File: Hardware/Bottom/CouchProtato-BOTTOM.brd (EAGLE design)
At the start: 0 parts

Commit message: update files
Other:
- board outline added: 160 x 100 mm
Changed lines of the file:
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@@
 <layer number="51" name="tDocu" color="7" fill="1" visible="yes" active="yes"/>
 <layer number="52" name="bDocu" color="7" fill="1" visible="yes" active="yes"/>
+<layer number="88" name="SimResults" color="9" fill="1" visible="no" active="no"/>
+<layer number="89" name="SimProbes" color="9" fill="1" visible="no" active="no"/>
+<layer number="90" name="Modules" color="5" fill="1" visible="no" active="no"/>
+<layer number="91" name="Nets" color="2" fill="1" visible="no" active="no"/>
+<layer number="92" name="Busses" color="1" fill="1" visible="no" active="no"/>
+<layer number="93" name="Pins" color="2" fill="1" visible="no" active="no"/>
+<layer number="94" name="Symbols" color="4" fill="1" visible="no" active="no"/>
+<layer number="95" name="Names" color="7" fill="1" visible="no" active="no"/>
+<layer number="96" name="Values" color="7" fill="1" visible="no" active="no"/>
+<layer number="97" name="Info" color="7" fill="1" visible="no" active="no"/>
+<layer number="98" name="Guide" color="6" fill="1" visible="no" active="no"/>
 </layers>
 <board>
 <plain>
+<wire x1="0" y1="0" x2="160" y2="0" width="0" layer="20"/>
+<wire x1="160" y1="0" x2="160" y2="100" width="0" layer="20"/>
+<wire x1="160" y1="100" x2="0" y2="100" width="0" layer="20"/>
+<wire x1="0" y1="100" x2="0" y2="0" width="0" layer="20"/>
 </plain>
 <attributes>

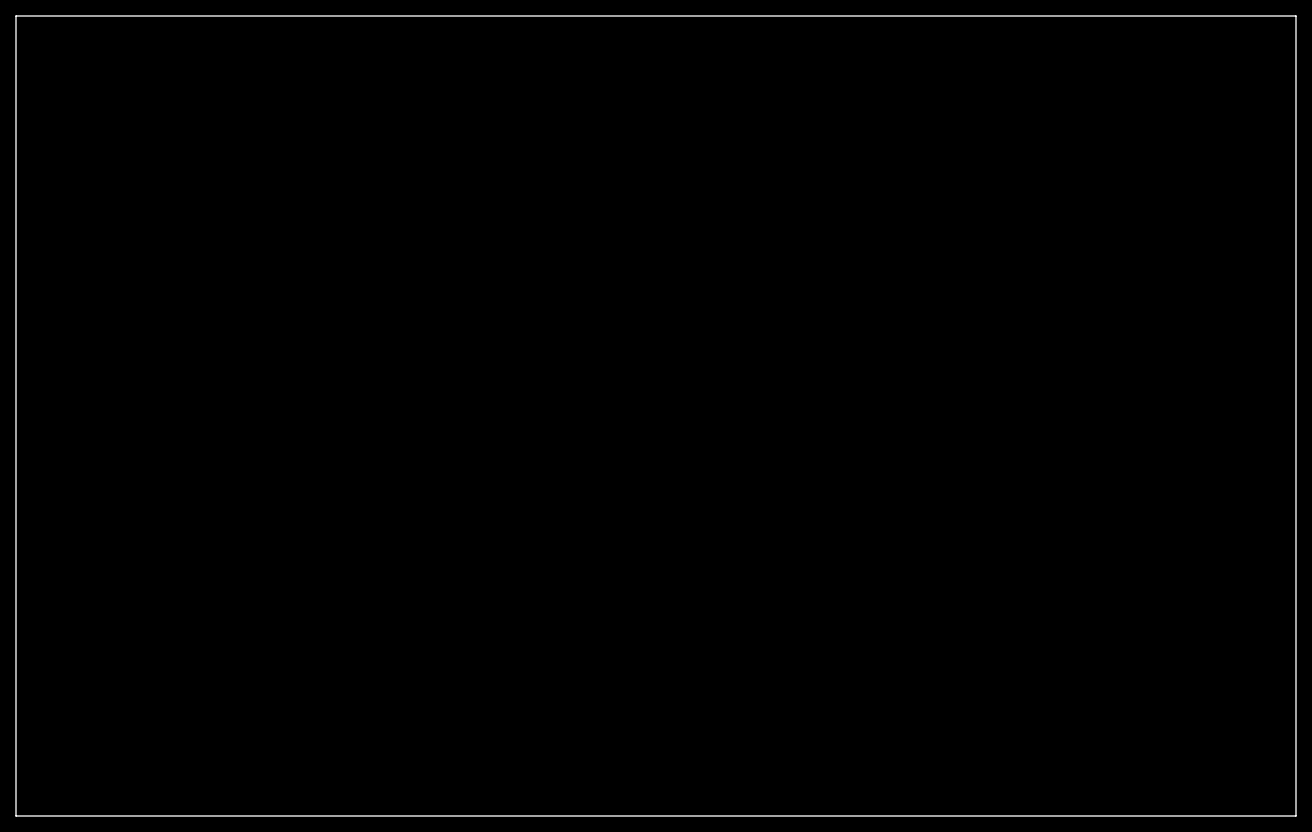
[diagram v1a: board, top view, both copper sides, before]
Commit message: Finished routing top and bottom boards
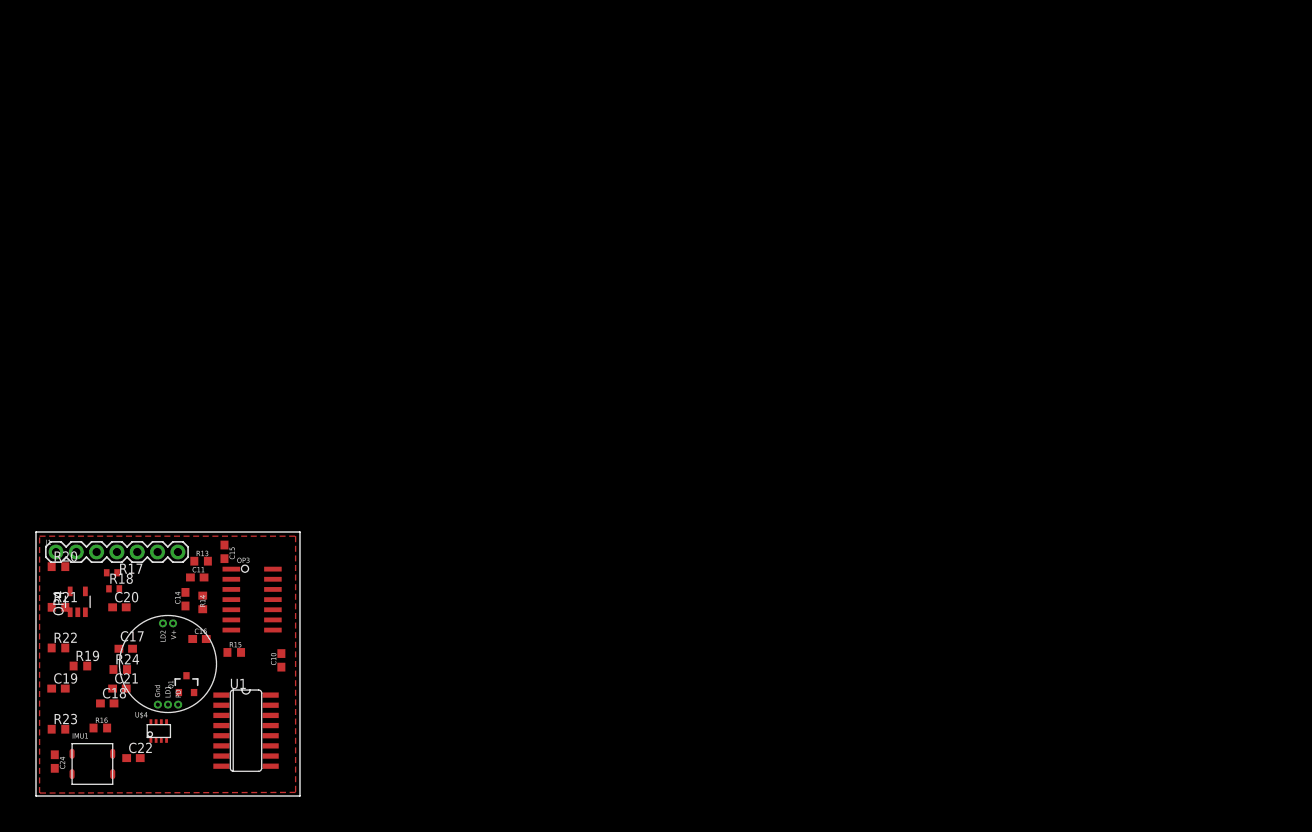
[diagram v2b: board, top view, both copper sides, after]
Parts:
- added C10, C11, C17, C18, C22, C24: 100n, LinnesLab-Passives:C0603
- added C14, C19: 2.2n, LinnesLab-Passives:C0603
- added C15, C16: 2.2u, LinnesLab-Passives:C0603
- added C20: 22u, LinnesLab-Passives:C0603
- added C21: 22n, LinnesLab-Passives:C0603
- added IMU1: LSM6DS3_CAST, LinnesLab-Sensors:LSM6DS3_CAST
- added J1: (no value), LinnesLab-Connectors:1X07
- added OP3: (no value), LinnesLab-AnalogIC:SO14
- added OP4: (no value), LinnesLab-AnalogIC:SOT23-5
- added Q1: (no value), LinnesLab-DiscreteSemi:SOT23-3
- added R13, R15, R19, R21: 220k, LinnesLab-Passives:R0603
- added R14, R22: 10M, LinnesLab-Passives:R0603
- added R16: (no value), LinnesLab-Passives:R0603
- added R17, R18: 10k, LinnesLab-Passives:R0402
- added R20, R23: 1M, LinnesLab-Passives:R0603
- added R24: 10k, LinnesLab-Passives:R0603
- added U$3: (no value), LinnesLab-Connectors:PPG.MODULE.2
- added U$4: AD5171, LinnesLab-DigitalIC:SOT-23-8
- added U1: AD5242-SO16, LinnesLab-DigitalIC:SO16
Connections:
- new net 3.3V: C11.2, C17.2, C18.2, C22.2, C24.2, IMU1.2, OP3.4, OP4.5, R13.2, R15.2, R17.2, U$3.V+, U$4.2, U$4.6, U1.5, U1.6
- new net A6/TIA: C10.2, C15.1, J1.5, OP4.1, U1.3
- new net A7/PPG: C21.2, J1.7, OP3.1, U1.14
- new net D29/LED.CTRL: J1.6, U$4.8
- new net G.A1: U1.2
- new net G.A2: U1.16
- new net G.O1: U1.1
- new net G.O2: U1.13
- new net G.W2: C21.1, OP3.2, R24.1, U1.15
- new net GND: C11.1, C17.1, C18.1, C22.1, C24.1, IMU1.1, OP3.11, OP4.2, OP4.3, Q1.2, R18.1, R19.1, R21.1, U$3.GND, U$4.3, U1.10, U1.11, U1.12, U1.9
- new net LED: Q1.3
- new net LED.C: U$3.LD1
- new net N$10: OP3.12, R17.1, R18.2
- new net N$13: C15.2, OP3.5, R13.1, R19.2
- new net N$15: C14.2, OP3.6, R14.1, R20.2
- new net N$16: C14.1, C16.1, OP3.7, R14.2
- new net N$17: C16.2, OP3.10, R15.1, R21.2
- new net N$18: C19.2, OP3.9, R22.1, R23.2
- new net N$19: C19.1, C20.1, OP3.8, R22.2
- new net N$20: C20.2, R24.2
- new net N$8: Q1.1, R16.2
- new net N$9: R16.1, U$4.1, U$4.7
- new net PD.C: C10.1, OP4.4, U$3.PD, U1.4
- new net SCL: IMU1.3, U$4.4, U1.7
- new net SDA: IMU1.4, U$4.5, U1.8
- new net VREF: OP3.13, OP3.14, OP3.3, R20.1, R23.1
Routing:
- added copper zone on layer 1, net 3.3V
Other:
- board size 160 x 100 mm -> 33 x 33 mm
